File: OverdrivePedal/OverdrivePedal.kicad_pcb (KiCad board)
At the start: 2 copper layers, 40.6 x 78.7 mm, 31 parts, among them J1 Conn_01x02, J2 Conn_01x02, J3 Conn_01x03, J4 Conn_01x03, J5 Conn_01x03, J6 Conn_01x02, Q1 DMG2301L, U1 TL071, U2 TC7662Bx0A, U3 MIC5233YM5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

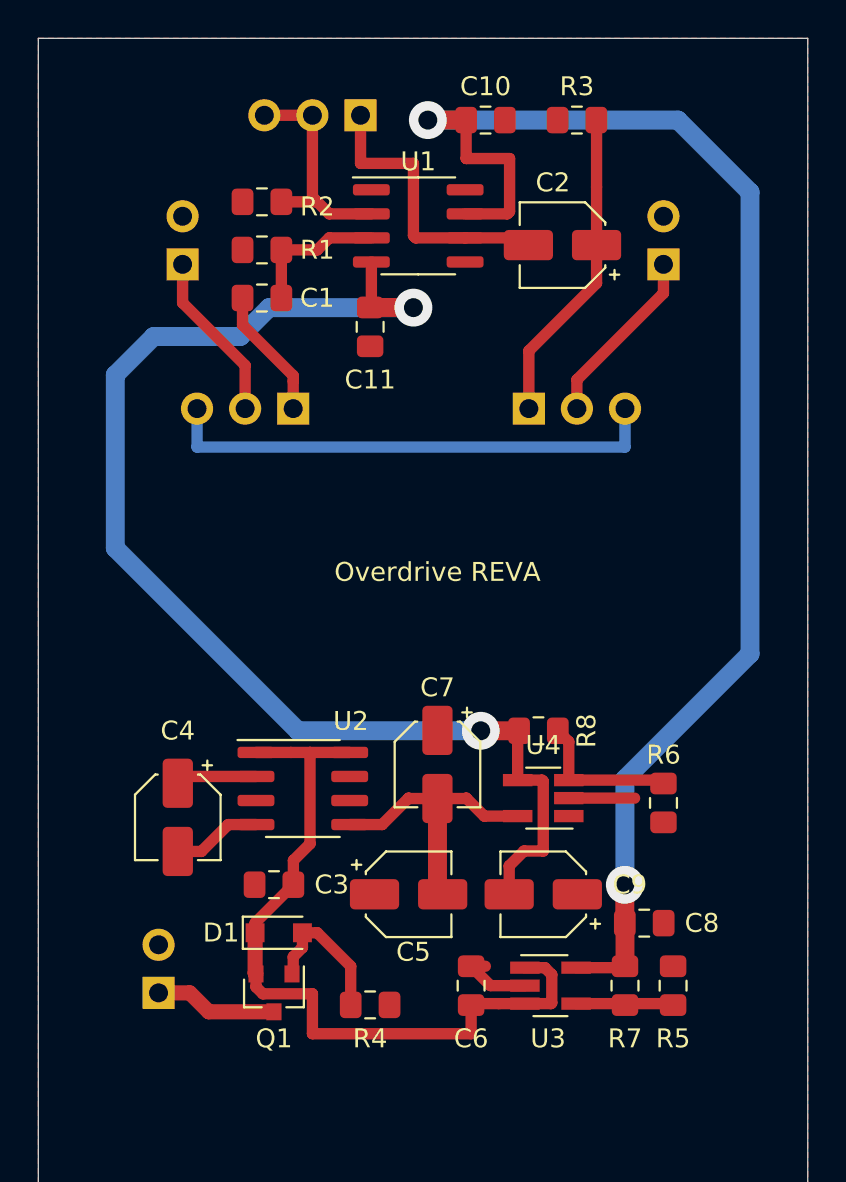
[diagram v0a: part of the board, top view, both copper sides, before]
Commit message: Replaced TL071 with TL072
UPDATED LAYOUT
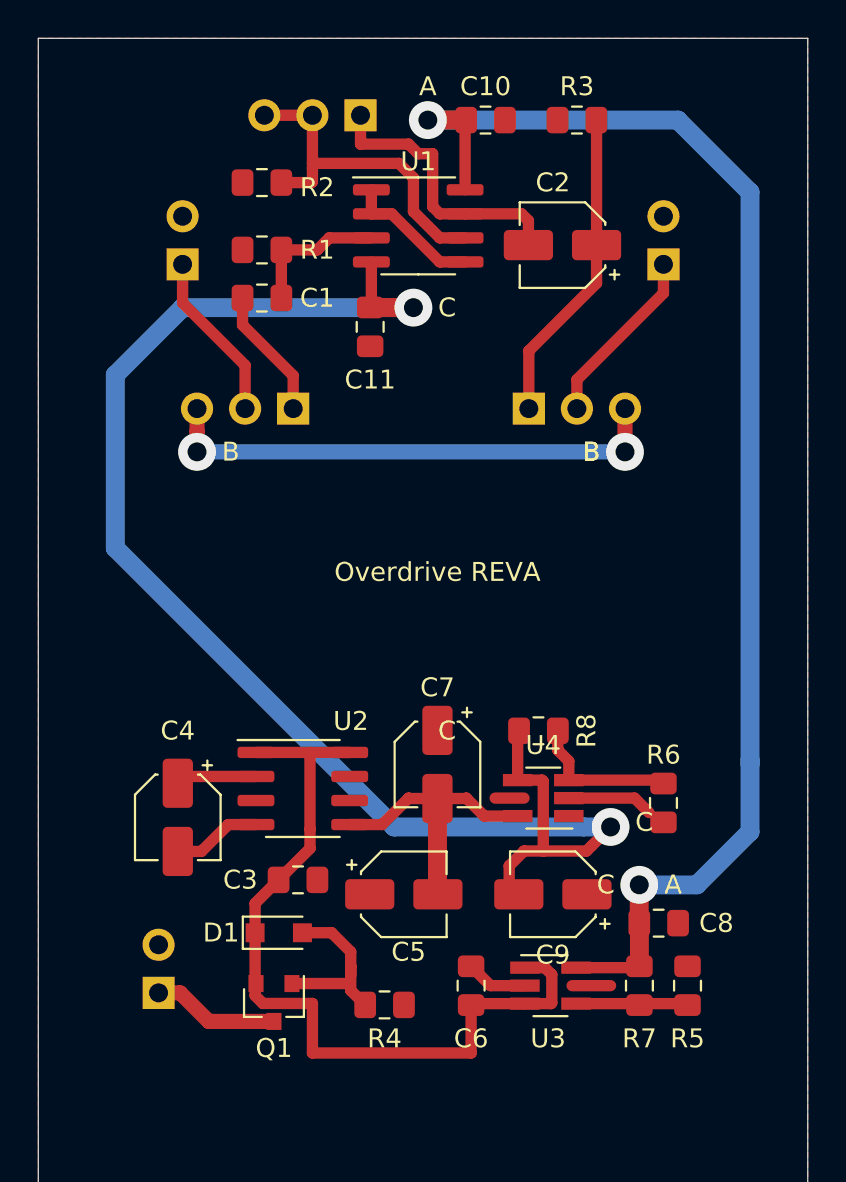
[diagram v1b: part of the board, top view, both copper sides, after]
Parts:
- U1: value TL071 -> TL072
- moved C3 1.30 mm to (115.3, 95.2), turned to 0 degrees
- moved R2 1.02 mm to (113.4, 58.4)
- moved C8 0.76 mm to (134.4, 97.5)
- moved R4 0.76 mm to (119.9, 101.9)
- moved R5 0.76 mm to (135.9, 100.8)
- moved R7 0.76 mm to (133.3, 100.8)
- moved Q1 0.51 mm to (114.0, 101.7)
- moved C9 0.51 mm to (128.8, 96.0)
- moved C5 0.25 mm to (120.9, 96.0)
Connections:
- U1 pad 2: Net-(J4-Pad2) -> Net-(U1-Pad1)
- U1 pad 5: Net-(U1-Pad5) -> Net-(U1-Pad1)
- U1 pad 6: Net-(C2-Pad2) -> Net-(J4-Pad2)
- U1 pad 7: +5V -> Net-(C2-Pad2)
- U1 pad 8: Net-(U1-Pad8) -> +5V
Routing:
- net -5V: track 68.0 -> 79.0 mm
- net Net-(U1-Pad1): track 0.00 -> 7.27 mm
- net Net-(J4-Pad2): track 12.2 -> 18.4 mm
- net +5V: track 76.4 -> 72.3 mm
- net (no net): track 0.00 -> 3.56 mm
- net /PosNeg5V_PSU/+9V_POL: track 41.1 -> 43.1 mm
- net Net-(D1-Pad2): track 7.73 -> 9.60 mm
- net Net-(J3-Pad3): track 26.7 -> 27.2 mm, vias 0 -> 2
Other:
- board text added: "A"
- board text added: "B"
- board text added: "C"

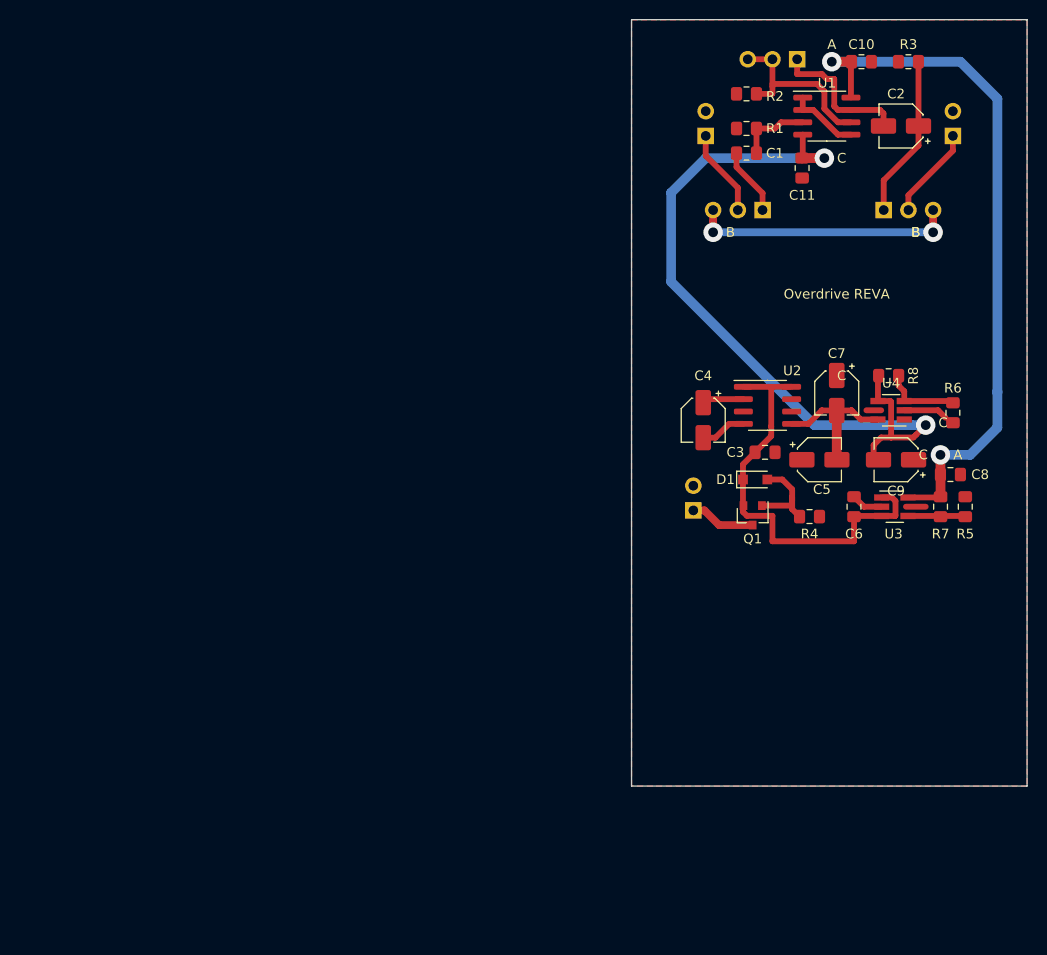
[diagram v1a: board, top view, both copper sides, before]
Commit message: Tested RevA Layout
- Removed AC coupling caps
- Reversed Switch connector
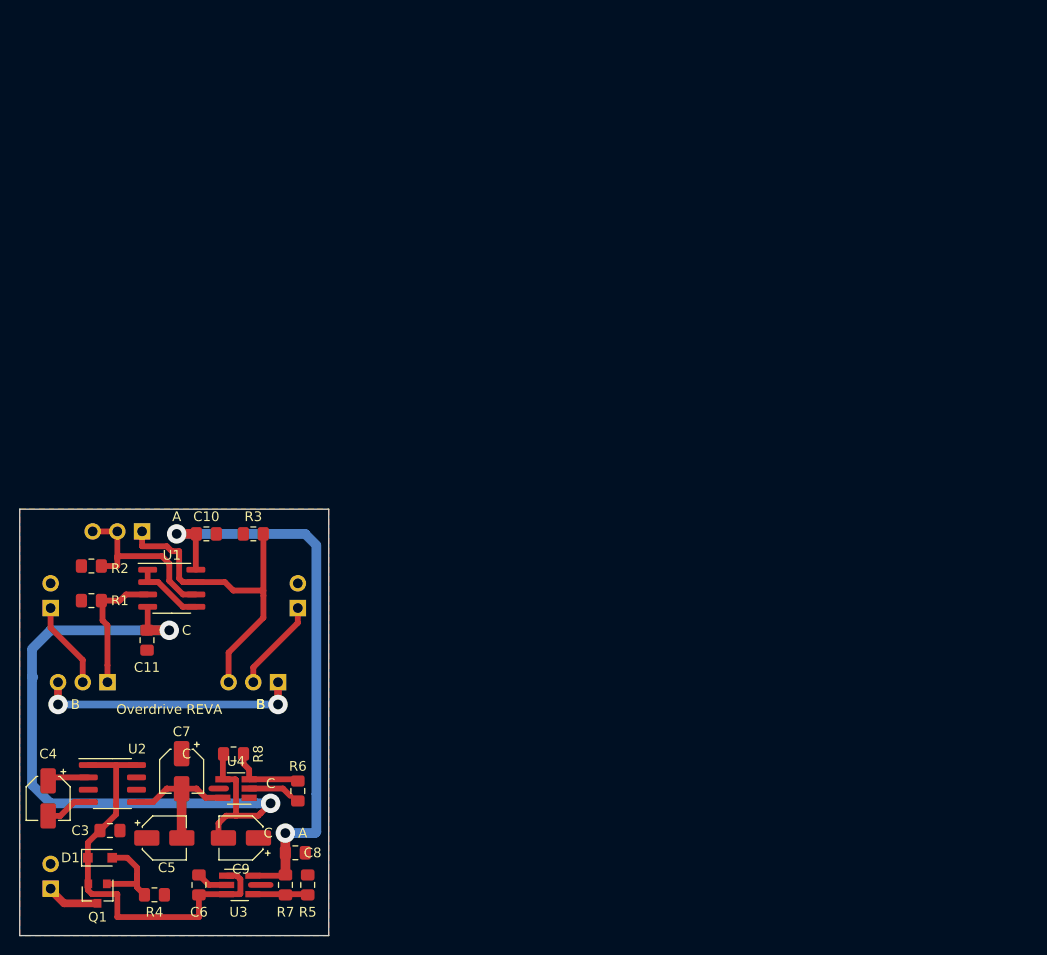
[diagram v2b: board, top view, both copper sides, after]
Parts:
- removed C1: 100nF, Capacitor_SMD:C_0805_2012Metric_Pad1.15x1.40mm_HandSolder
- removed C2: 15uF, Capacitor_SMD:CP_Elec_4x5.7
- R5: value 1K -> 330R
- R7: value 330R -> 1K
- moved C10 83.0 mm to (57.9, 103.6)
- moved C11 83.0 mm to (51.8, 114.6)
- moved J1 83.0 mm to (41.9, 111.3)
- moved J3 83.0 mm to (47.8, 118.9)
- moved J4 83.0 mm to (51.3, 103.4)
- moved J6 83.0 mm to (67.3, 111.3)
- moved R1 83.0 mm to (46.1, 110.5)
- moved R2 83.0 mm to (46.1, 106.9)
- moved R3 83.0 mm to (62.7, 103.6)
- moved U1 83.0 mm to (54.4, 109.2)
- moved J5 78.9 mm to (65.3, 118.9), turned to 90 degrees
- moved R5 77.9 mm to (68.3, 139.7)
- moved C8 77.7 mm to (67.1, 136.4)
- moved C3 77.7 mm to (48.0, 134.1)
- moved C4 77.7 mm to (41.7, 130.8)
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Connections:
- J3 pad 1: Net-(C1-Pad1) -> Net-(J3-Pad1)
- J4 pad 1: Net-(C2-Pad2) -> Net-(J4-Pad1)
- J5 pad 1: Net-(C2-Pad1) -> Net-(J3-Pad3)
- J5 pad 3: Net-(J3-Pad3) -> Net-(J4-Pad1)
- R1 pad 1: Net-(C1-Pad2) -> Net-(J3-Pad1)
- R3 pad 1: Net-(C2-Pad1) -> Net-(J4-Pad1)
- U1 pad 3: Net-(C1-Pad2) -> Net-(J3-Pad1)
- U1 pad 7: Net-(C2-Pad2) -> Net-(J4-Pad1)
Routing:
- net Net-(J4-Pad1): track 0.00 -> 34.0 mm
- net Net-(C2-Pad1): track 16.5 -> 0.00 mm
- net Net-(C2-Pad2): track 15.2 -> 0.00 mm
- net Net-(J3-Pad1): track 0.00 -> 13.7 mm
- net +5V: track 72.3 -> 59.9 mm
- net Net-(C1-Pad2): track 7.56 -> 0.00 mm
- net Net-(C1-Pad1): track 6.95 -> 0.00 mm
- net -5V: track 79.0 -> 74.6 mm
- net /PosNeg5V_PSU/+9V_POL: track 43.1 -> 42.6 mm
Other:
- board size 40.6 x 78.7 mm -> 31.8 x 43.8 mm

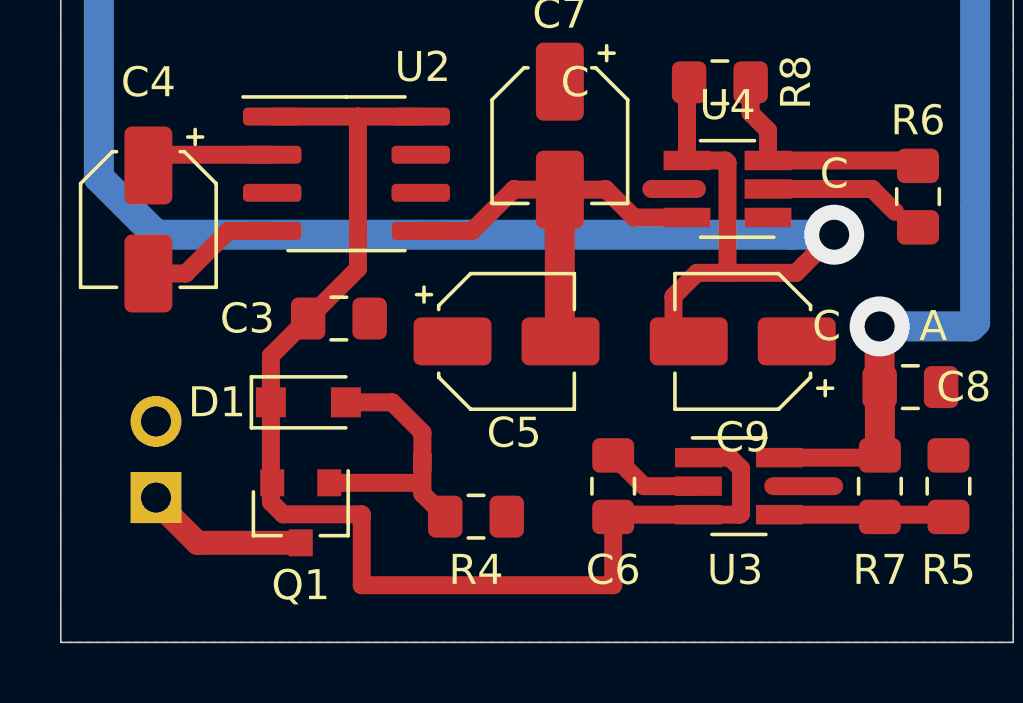
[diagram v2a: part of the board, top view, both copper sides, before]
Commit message: changed polarity protection mosfet to schotky diode
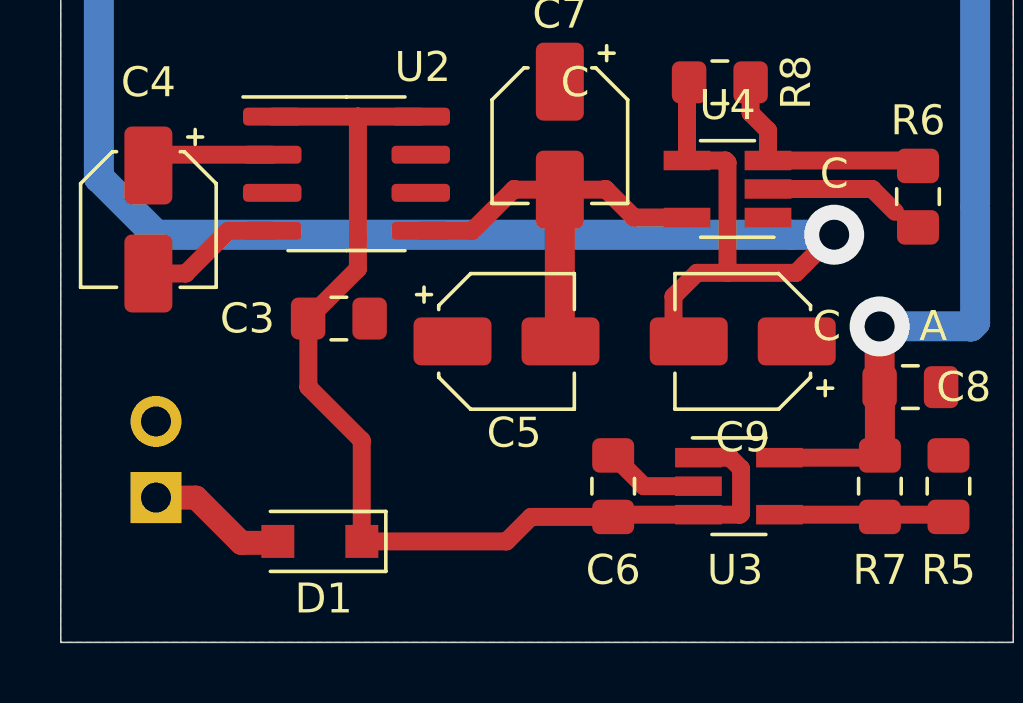
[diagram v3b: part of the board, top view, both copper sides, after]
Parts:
- removed Q1: DMG2301L, Package_TO_SOT_SMD:SOT-23
- removed R4: 100K, Resistor_SMD:R_0805_2012Metric_Pad1.15x1.40mm_HandSolder
- D1: value 10V -> D_Schottky; footprint Diode_SMD:D_SOD-323_HandSoldering -> Diode_SMD:D_SOD-123F
- moved D1 4.65 mm to (47.4, 141.5), turned to 180 degrees
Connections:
- D1 pad 2: Net-(D1-Pad2) -> /PosNeg5V_PSU/+9V_IN
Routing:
- net Net-(D1-Pad2): track 9.60 -> 0.00 mm
- net /PosNeg5V_PSU/+9V_POL: track 42.6 -> 36.6 mm
- net (no net): track 3.56 -> 0.00 mm

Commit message: updates
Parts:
- moved C8 5.71 mm to (69.1, 141.7), turned to 270 degrees
- moved R6 4.20 mm to (65.5, 126.2), turned to 0 degrees
- moved R5 3.88 mm to (65.0, 141.7), turned to 270 degrees
- moved R3 2.74 mm to (63.8, 106.2), turned to 90 degrees
- moved J2 2.62 mm to (44.5, 140.7), turned to 90 degrees
- moved D1 2.55 mm to (49.8, 140.7)
- moved R7 1.02 mm to (67.1, 139.7)
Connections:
- J1 pad 2: GND -> GNDS
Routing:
- net GNDS: track 7.82 -> 78.1 mm, vias 0 -> 1
- net +5V: track 59.9 -> 67.0 mm
- net Net-(J4-Pad1): track 34.0 -> 30.7 mm
- net /PosNeg5V_PSU/+9V_POL: track 36.6 -> 34.1 mm
- net /PosNeg5V_PSU/+9V_IN: track 4.83 -> 3.93 mm
- net Net-(R5-Pad1): track 5.16 -> 4.40 mm
- net Net-(R6-Pad1): track 7.92 -> 7.18 mm
- added copper zone on B.Cu, net GNDS
- removed copper zone on F.Cu, net GNDS
